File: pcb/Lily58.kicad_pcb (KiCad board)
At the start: 2 copper layers, 142.5 x 106.3 mm, 124 parts, among them J2 4PIN, J3 Conn_01x06_Female, J4 Conn_01x06_Female, P1 i2c_pin, P2 i2c_pin, SW1 SW_PUSH, SW10 SW_PUSH, SW11 SW_PUSH, SW12 SW_PUSH, SW13 SW_PUSH, SW14 SW_PUSH, SW15 SW_PUSH, SW16 SW_PUSH, SW17 SW_PUSH, SW18 SW_PUSH, SW19 SW_PUSH, SW2 SW_PUSH, SW20 SW_PUSH, SW21 SW_PUSH, SW22 SW_PUSH, SW23 SW_PUSH, SW24 SW_PUSH, SW25 SW_PUSH, SW26 SW_PUSH, SW27 SW_PUSH, SW28 SW_PUSH, SW29 SW_PUSH, SW3 SW_PUSH, SW4 SW_PUSH, SW5 SW_PUSH, SW6 SW_PUSH, SW7 SW_PUSH, SW8 SW_PUSH, SW9 SW_PUSH, U1 ProMicro

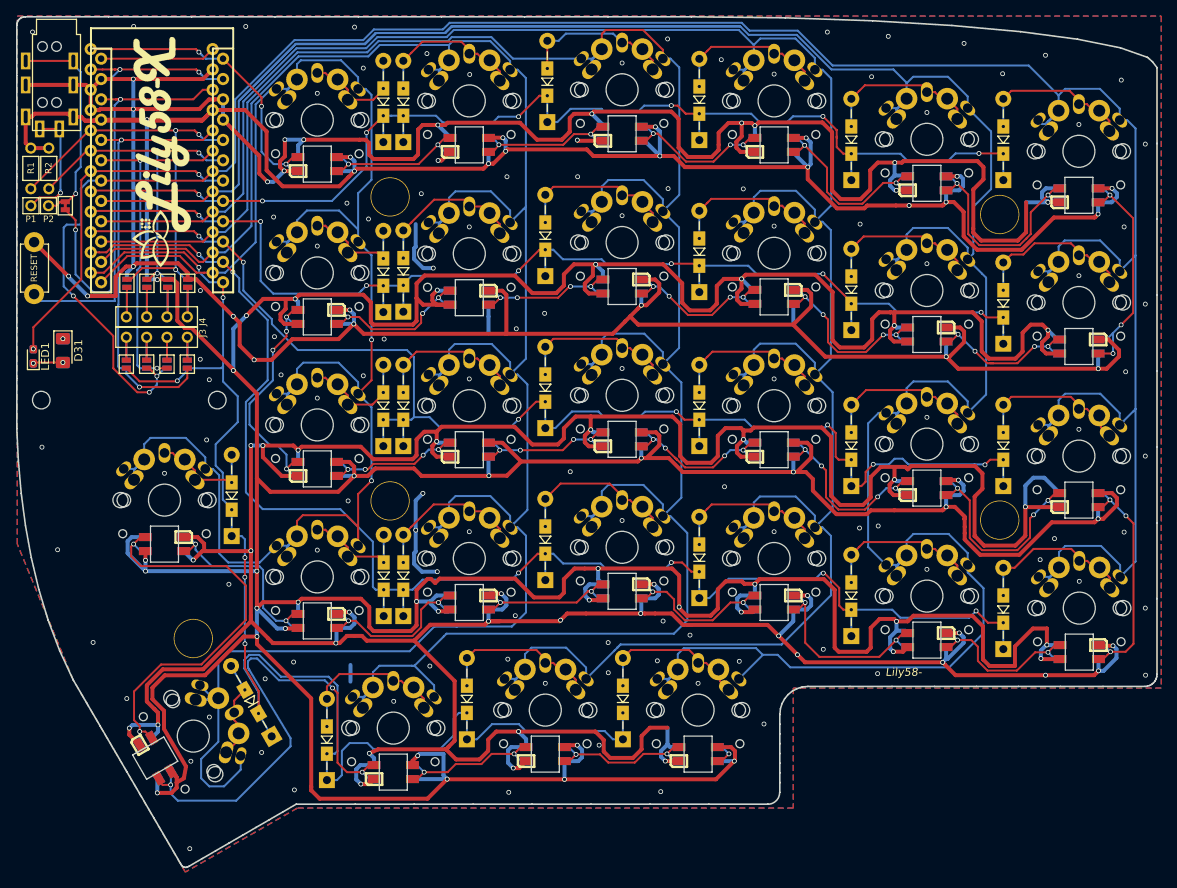
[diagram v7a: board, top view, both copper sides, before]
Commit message: add sk6812mini
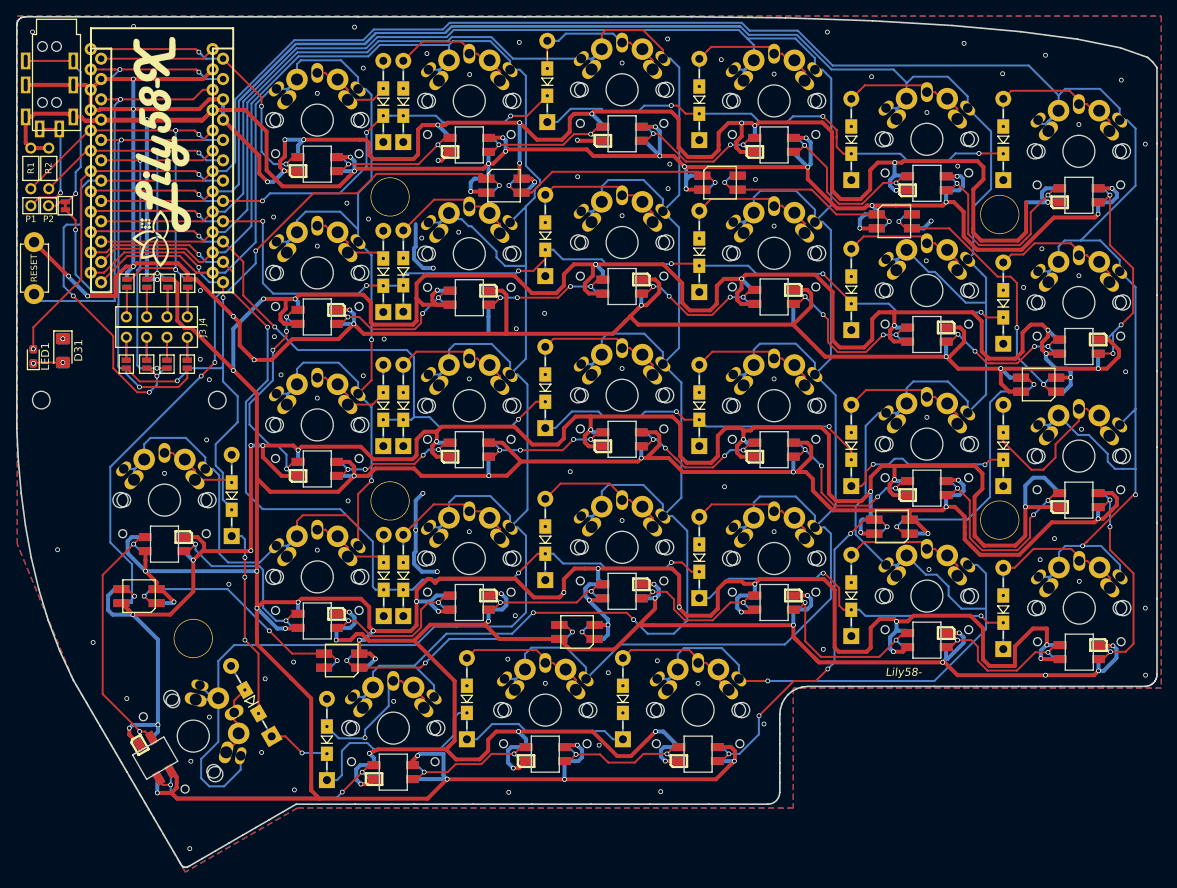
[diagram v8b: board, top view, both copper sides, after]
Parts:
- added L30: SK6812mini, Lily58-footprint:SK6812MINI_underglow_rev, F.Cu at (192.6, 62.7)
- added L31: SK6812mini, Lily58-footprint:SK6812MINI_underglow_rev, F.Cu at (170.8, 57.8)
- added L32: SK6812mini, Lily58-footprint:SK6812MINI_underglow_rev, F.Cu at (143.8, 58.2)
- added L33: SK6812mini, Lily58-footprint:SK6812MINI_underglow_rev, F.Cu at (98.2, 109.5)
- added L34: SK6812mini, Lily58-footprint:SK6812MINI_underglow_rev, F.Cu at (123.5, 117.6)
- added L35: SK6812mini, Lily58-footprint:SK6812MINI_underglow_rev, F.Cu at (153.0, 114.0)
- added L36: SK6812mini, Lily58-footprint:SK6812MINI_underglow_rev, F.Cu at (210.7, 83.1)
- added L37: SK6812mini, Lily58-footprint:SK6812MINI_underglow_rev, F.Cu at (192.3, 100.8)
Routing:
- net Net-(L32-Pad1): track 0.00 -> 92.2 mm, vias 0 -> 5
- net VCC: track 1031.0 -> 1084.2 mm, vias 55 -> 66
- net Net-(L29-Pad1): track 3.64 -> 46.0 mm, vias 1 -> 5
- net Net-(L30-Pad3): track 0.00 -> 38.0 mm, vias 0 -> 3
- net Net-(L36-Pad3): track 0.00 -> 33.8 mm, vias 0 -> 2
- net Net-(L34-Pad1): track 0.00 -> 31.4 mm, vias 0 -> 3
- net Net-(L26-Pad1): track 63.4 -> 32.8 mm
- net Net-(L31-Pad1): track 0.00 -> 30.2 mm, vias 0 -> 2
- net Net-(L33-Pad1): track 0.00 -> 29.2 mm, vias 0 -> 3
- net Net-(L30-Pad1): track 0.00 -> 26.5 mm, vias 0 -> 2
- net row4: track 181.0 -> 158.7 mm, vias 6 -> 7
- net GND: track 1028.0 -> 1050.3 mm, vias 166 -> 161
- net Net-(L25-Pad1): track 51.4 -> 33.5 mm
- net Net-(D18-Pad2): track 20.2 -> 27.0 mm
- net col0: track 316.7 -> 312.5 mm, vias 3 -> 5
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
